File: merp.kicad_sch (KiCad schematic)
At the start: 25 parts, among them J1 A, J10 -12V, J11 F, J12 Conn_01x04_Male, J2 B, J3 C, J4 D, J5 E, J6 IO1, J7 IO2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

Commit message: add gerbers
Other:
- company: Crankery -> Dave Hamilton
- title: Eurorack Power Bus -> Merp: Modular Eurorack Powerbus
- moved on the sheet: C1, C2, C3, D1, D2, D3, J10, J12, J7, J8, J9, R1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

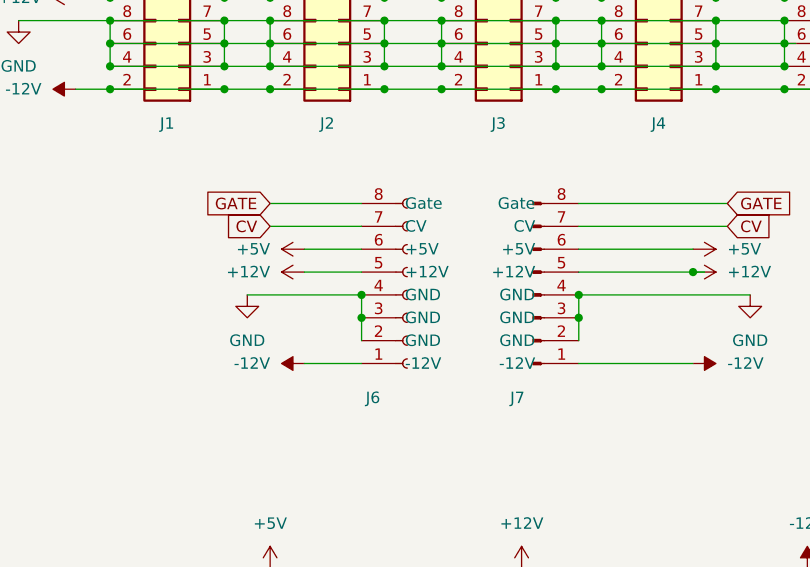
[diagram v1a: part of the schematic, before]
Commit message: fix url on board
upgrade to kicad 7
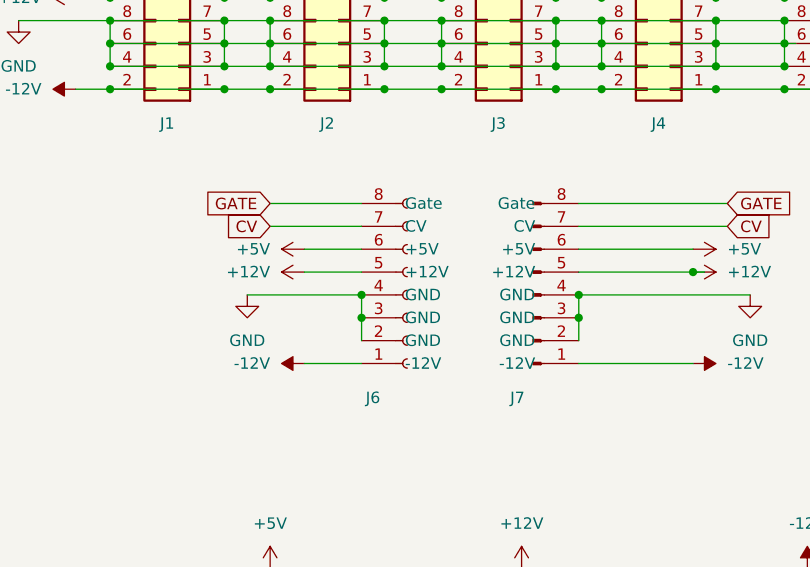
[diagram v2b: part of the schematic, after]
